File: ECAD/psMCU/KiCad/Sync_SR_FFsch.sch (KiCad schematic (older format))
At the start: 8 parts, among them U101 SN74LVC1G32DCK, U102 SN74LVC1G08DCK, U114 SN74LVC1G175DCK, U96 SN74LVC1G04DCK

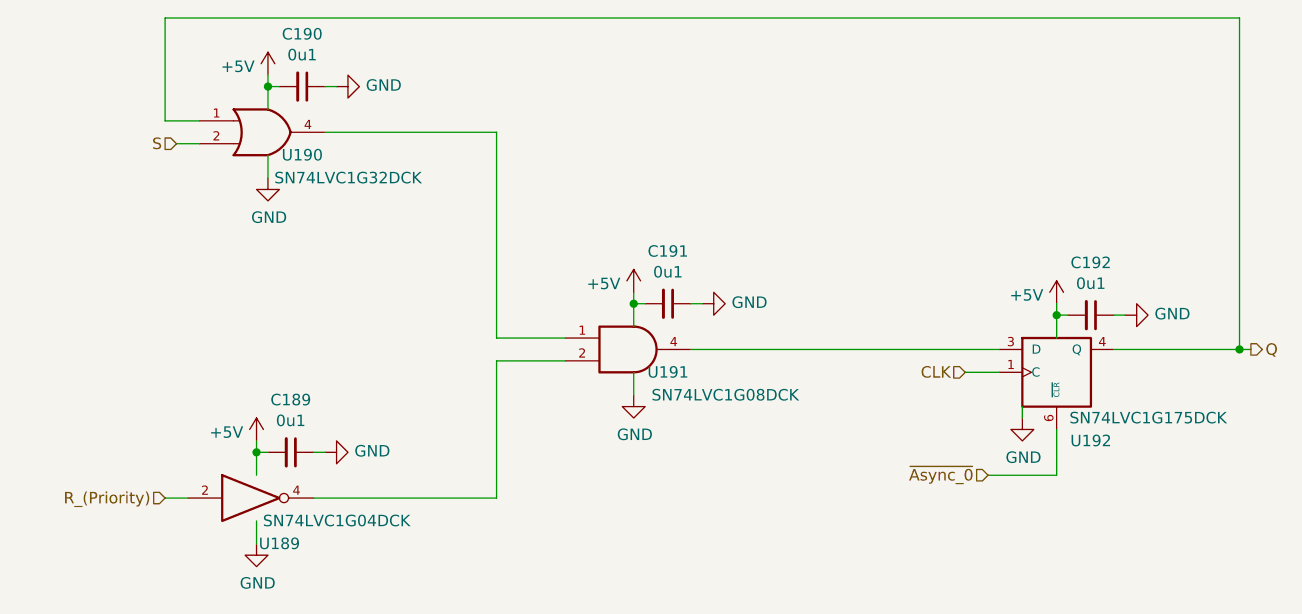
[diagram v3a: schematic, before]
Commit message: Sch: Increased RAM page count, changed SYS registers
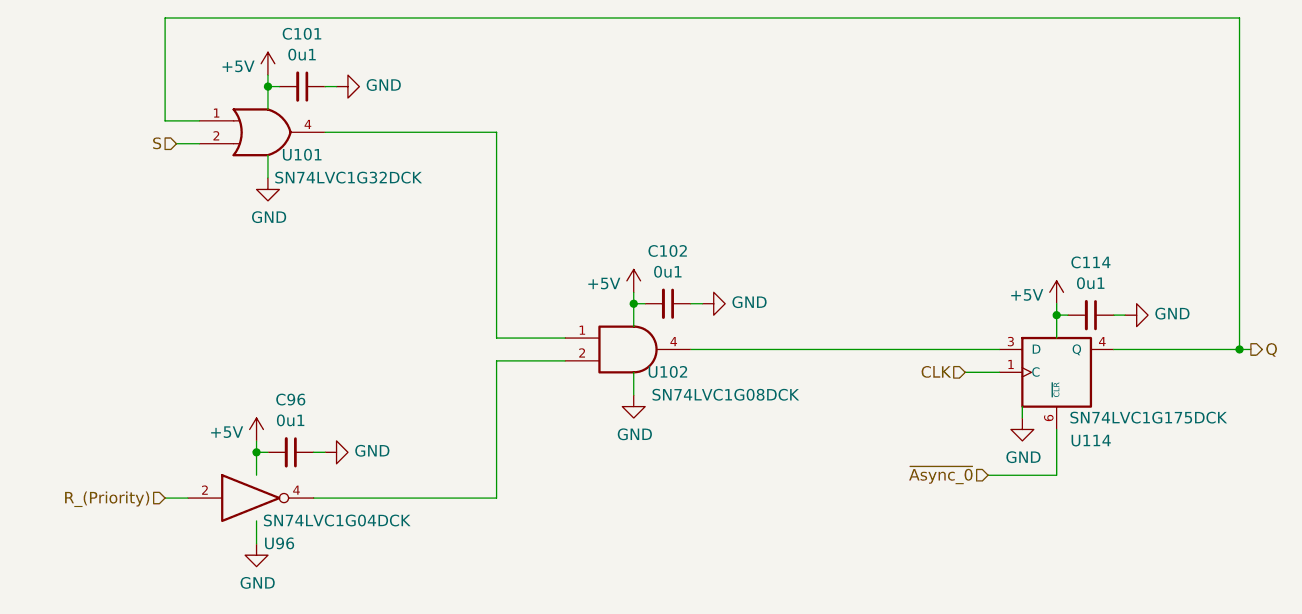
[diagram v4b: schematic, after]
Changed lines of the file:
@@
 $Descr A4 11693 8268
 encoding utf-8
-Sheet 22 96
+Sheet 20 96
 Title "psMCU"
 Date "2022-02-13"
@@
 AR Path="/60E33DBC/5FD12DEC/60B2DD5B/60B01E21" Ref="C188"  Part="1"
 AR Path="/60E33DBC/5FD12DEC/60B2E59A/60B01E21" Ref="C192"  Part="1"
-F 0 "C192" V 6771 3150 50  0000 C CNN
+F 0 "C114" V 6771 3150 50  0000 C CNN
 F 1 "0u1" V 6862 3150 50  0000 C CNN
 F 2 "NoRef_Footprints:C_0603_1608Metric_NoRef" H 7000 3150 50  0001 C CNN
@@
 AR Path="/60E33DBC/5FD12DEC/60B2DD5B/60B01E61" Ref="U188"  Part="1"
 AR Path="/60E33DBC/5FD12DEC/60B2E59A/60B01E61" Ref="U192"  Part="1"
-F 0 "U192" H 7000 3100 50  0000 C CNN
+F 0 "U114" H 7000 3100 50  0000 C CNN
 F 1 "SN74LVC1G175DCK" H 7250 3200 50  0000 C CNN
 F 2 "Package_TO_SOT_SMD:SOT-363_SC-70-6" H 6850 3400 50  0001 C CNN
@@
 AR Path="/60E33DBC/5FD12DEC/60B2DD5B/60B07E89" Ref="U152"  Part="1"
 AR Path="/60E33DBC/5FD12DEC/60B2E59A/60B07E89" Ref="U191"  Part="1"
-F 0 "U191" H 5150 3200 50  0000 C CNN
+F 0 "U102" H 5150 3200 50  0000 C CNN
 F 1 "SN74LVC1G08DCK" H 5400 3100 50  0000 C CNN
 F 2 "Package_TO_SOT_SMD:SOT-353_SC-70-5" H 5000 3300 50  0001 C CNN
@@
 AR Path="/60E33DBC/5FD12DEC/60B2DD5B/60B07E9D" Ref="C151"  Part="1"
 AR Path="/60E33DBC/5FD12DEC/60B2E59A/60B07E9D" Ref="C191"  Part="1"
-F 0 "C191" V 4921 3100 50  0000 C CNN
+F 0 "C102" V 4921 3100 50  0000 C CNN
 F 1 "0u1" V 5012 3100 50  0000 C CNN
 F 2 "NoRef_Footprints:C_0603_1608Metric_NoRef" H 5150 3100 50  0001 C CNN
@@
 AR Path="/60E33DBC/5FD12DEC/60B2DD5B/60B07EAD" Ref="U150"  Part="1"
 AR Path="/60E33DBC/5FD12DEC/60B2E59A/60B07EAD" Ref="U190"  Part="1"
-F 0 "U190" H 3550 2250 50  0000 C CNN
+F 0 "U101" H 3550 2250 50  0000 C CNN
 F 1 "SN74LVC1G32DCK" H 3750 2150 50  0000 C CNN
 F 2 "Package_TO_SOT_SMD:SOT-353_SC-70-5" H 3400 2350 50  0001 C CNN
@@
 AR Path="/60E33DBC/5FD12DEC/60B2DD5B/60B07EC1" Ref="C150"  Part="1"
 AR Path="/60E33DBC/5FD12DEC/60B2E59A/60B07EC1" Ref="C190"  Part="1"
-F 0 "C190" V 3321 2150 50  0000 C CNN
+F 0 "C101" V 3321 2150 50  0000 C CNN
 F 1 "0u1" V 3412 2150 50  0000 C CNN
 F 2 "NoRef_Footprints:C_0603_1608Metric_NoRef" H 3550 2150 50  0001 C CNN
@@
 AR Path="/60E33DBC/5FD12DEC/60B2DD5B/60B07ED1" Ref="U115"  Part="1"
 AR Path="/60E33DBC/5FD12DEC/60B2E59A/60B07ED1" Ref="U189"  Part="1"
-F 0 "U189" H 3450 3750 50  0000 C CNN
+F 0 "U96" H 3450 3750 50  0000 C CNN
 F 1 "SN74LVC1G04DCK" H 3700 3850 50  0000 C CNN
 F 2 "Package_TO_SOT_SMD:SOT-353_SC-70-5" H 3350 3950 50  0001 C CNN
@@
 AR Path="/60E33DBC/5FD12DEC/60B2DD5B/60B07EDE" Ref="C115"  Part="1"
 AR Path="/60E33DBC/5FD12DEC/60B2E59A/60B07EDE" Ref="C189"  Part="1"
-F 0 "C189" V 3271 3750 50  0000 C CNN
+F 0 "C96" V 3271 3750 50  0000 C CNN
 F 1 "0u1" V 3362 3750 50  0000 C CNN
 F 2 "NoRef_Footprints:C_0603_1608Metric_NoRef" H 3500 3750 50  0001 C CNN

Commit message: Sch: Improved Clk/Reset distribution, moved to global labels
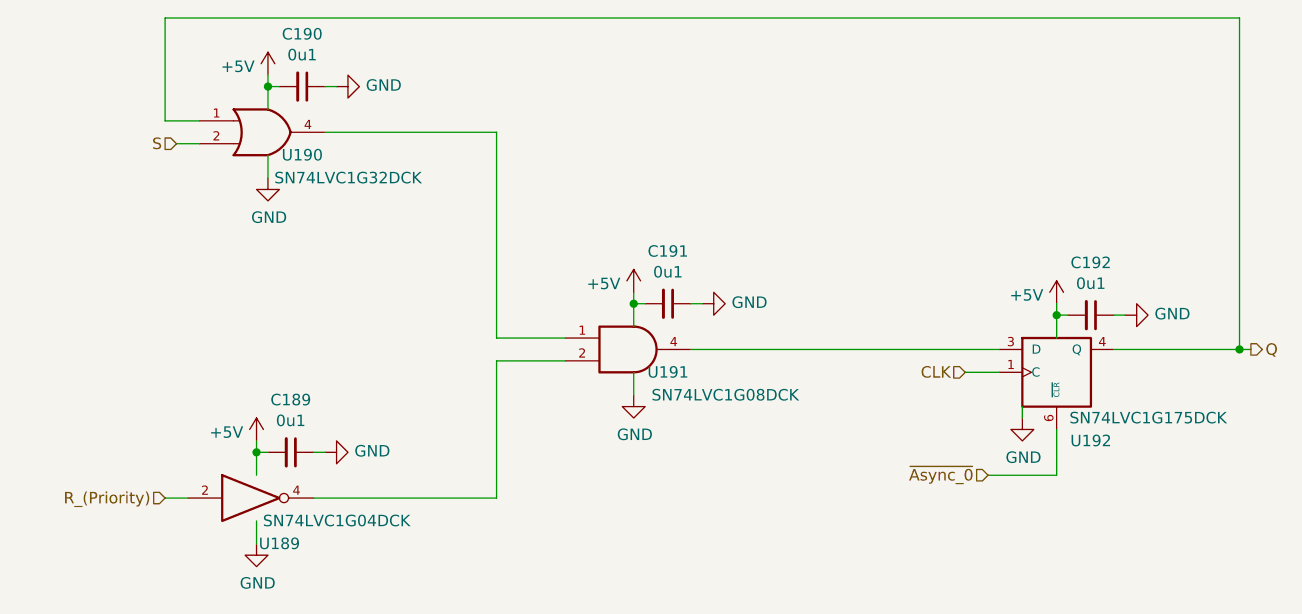
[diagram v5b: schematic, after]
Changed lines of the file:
@@
 $Descr A4 11693 8268
 encoding utf-8
-Sheet 20 96
+Sheet 22 97
 Title "psMCU"
 Date "2022-02-13"
@@
 AR Path="/60E33DBC/5FD12DEC/60B2DD5B/60B01E21" Ref="C188"  Part="1"
 AR Path="/60E33DBC/5FD12DEC/60B2E59A/60B01E21" Ref="C192"  Part="1"
-F 0 "C114" V 6771 3150 50  0000 C CNN
+F 0 "C192" V 6771 3150 50  0000 C CNN
 F 1 "0u1" V 6862 3150 50  0000 C CNN
 F 2 "NoRef_Footprints:C_0603_1608Metric_NoRef" H 7000 3150 50  0001 C CNN
@@
 AR Path="/60E33DBC/5FD12DEC/60B2DD5B/60B01E61" Ref="U188"  Part="1"
 AR Path="/60E33DBC/5FD12DEC/60B2E59A/60B01E61" Ref="U192"  Part="1"
-F 0 "U114" H 7000 3100 50  0000 C CNN
+F 0 "U192" H 7000 3100 50  0000 C CNN
 F 1 "SN74LVC1G175DCK" H 7250 3200 50  0000 C CNN
 F 2 "Package_TO_SOT_SMD:SOT-363_SC-70-6" H 6850 3400 50  0001 C CNN
@@
 AR Path="/60E33DBC/5FD12DEC/60B2DD5B/60B07E89" Ref="U152"  Part="1"
 AR Path="/60E33DBC/5FD12DEC/60B2E59A/60B07E89" Ref="U191"  Part="1"
-F 0 "U102" H 5150 3200 50  0000 C CNN
+F 0 "U191" H 5150 3200 50  0000 C CNN
 F 1 "SN74LVC1G08DCK" H 5400 3100 50  0000 C CNN
 F 2 "Package_TO_SOT_SMD:SOT-353_SC-70-5" H 5000 3300 50  0001 C CNN
@@
 AR Path="/60E33DBC/5FD12DEC/60B2DD5B/60B07E9D" Ref="C151"  Part="1"
 AR Path="/60E33DBC/5FD12DEC/60B2E59A/60B07E9D" Ref="C191"  Part="1"
-F 0 "C102" V 4921 3100 50  0000 C CNN
+F 0 "C191" V 4921 3100 50  0000 C CNN
 F 1 "0u1" V 5012 3100 50  0000 C CNN
 F 2 "NoRef_Footprints:C_0603_1608Metric_NoRef" H 5150 3100 50  0001 C CNN
@@
 AR Path="/60E33DBC/5FD12DEC/60B2DD5B/60B07EAD" Ref="U150"  Part="1"
 AR Path="/60E33DBC/5FD12DEC/60B2E59A/60B07EAD" Ref="U190"  Part="1"
-F 0 "U101" H 3550 2250 50  0000 C CNN
+F 0 "U190" H 3550 2250 50  0000 C CNN
 F 1 "SN74LVC1G32DCK" H 3750 2150 50  0000 C CNN
 F 2 "Package_TO_SOT_SMD:SOT-353_SC-70-5" H 3400 2350 50  0001 C CNN
@@
 AR Path="/60E33DBC/5FD12DEC/60B2DD5B/60B07EC1" Ref="C150"  Part="1"
 AR Path="/60E33DBC/5FD12DEC/60B2E59A/60B07EC1" Ref="C190"  Part="1"
-F 0 "C101" V 3321 2150 50  0000 C CNN
+F 0 "C190" V 3321 2150 50  0000 C CNN
 F 1 "0u1" V 3412 2150 50  0000 C CNN
 F 2 "NoRef_Footprints:C_0603_1608Metric_NoRef" H 3550 2150 50  0001 C CNN
@@
 AR Path="/60E33DBC/5FD12DEC/60B2DD5B/60B07ED1" Ref="U115"  Part="1"
 AR Path="/60E33DBC/5FD12DEC/60B2E59A/60B07ED1" Ref="U189"  Part="1"
-F 0 "U96" H 3450 3750 50  0000 C CNN
+F 0 "U189" H 3450 3750 50  0000 C CNN
 F 1 "SN74LVC1G04DCK" H 3700 3850 50  0000 C CNN
 F 2 "Package_TO_SOT_SMD:SOT-353_SC-70-5" H 3350 3950 50  0001 C CNN
@@
 AR Path="/60E33DBC/5FD12DEC/60B2DD5B/60B07EDE" Ref="C115"  Part="1"
 AR Path="/60E33DBC/5FD12DEC/60B2E59A/60B07EDE" Ref="C189"  Part="1"
-F 0 "C96" V 3271 3750 50  0000 C CNN
+F 0 "C189" V 3271 3750 50  0000 C CNN
 F 1 "0u1" V 3362 3750 50  0000 C CNN
 F 2 "NoRef_Footprints:C_0603_1608Metric_NoRef" H 3500 3750 50  0001 C CNN
